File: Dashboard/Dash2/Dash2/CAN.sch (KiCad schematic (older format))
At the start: 20 parts, among them J201 CAN_OUT, J202 CAN_IN, U201 ADM3055E, U202 CDSOT23-T24CAN

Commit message: Add complete layout of the board
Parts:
- C201, C206: Mouser Part Number (none) -> 80-C0805C106K8RAUTO
- C202, C203, C207: Mouser Part Number (none) -> 80-C0805C104K3R
- C204, C208: Mouser Part Number (none) -> 80-C0805X103K1R3316
- C205: Mouser Part Number (none) -> 80-C0805C224J1RECTU
- L201, L202: Mouser Part Number (none) -> 963-BK2125LM182-T
- R201: Mouser Part Number (none) -> 71-CRCW08050000Z0EAC
- R202, R203: Mouser Part Number (none) -> 71-CRCW080559R0FKEA
- U202: Mouser Part Number (none) -> 652-CDSOT23-T24CAN
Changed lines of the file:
@@
 EESchema Schematic File Version 4
-LIBS:Dash2-cache
-EELAYER 26 0
+EELAYER 30 0
 EELAYER END
 $Descr A4 11693 8268
@@
 F 2 "Resistor_SMD:R_0805_2012Metric" V 8130 3550 50  0001 C CNN
 F 3 "" H 8200 3550 50  0001 C CNN
+F 4 "71-CRCW080559R0FKEA" H 8200 3550 50  0001 C CNN "Mouser Part Number"
 	1    8200 3550
 	1    0    0    -1
@@
 F 2 "Resistor_SMD:R_0805_2012Metric" V 7930 3550 50  0001 C CNN
 F 3 "" H 8000 3550 50  0001 C CNN
+F 4 "71-CRCW080559R0FKEA" H 8000 3550 50  0001 C CNN "Mouser Part Number"
 	1    8000 3550
 	1    0    0    -1
@@
 F 2 "Capacitor_SMD:C_0805_2012Metric" H 2150 3350 50  0001 C CNN
 F 3 "" H 2150 3350 50  0001 C CNN
+F 4 "80-C0805C106K8RAUTO " H 2150 3350 50  0001 C CNN "Mouser Part Number"
 	1    2150 3350
 	1    0    0    -1
@@
 F 1 "0.1uF" H 2510 3270 50  0000 L CNN
 F 2 "Capacitor_SMD:C_0805_2012Metric" H 2500 3350 50  0001 C CNN
-F 3 "" H 2500 3350 50  0001 C CNN
+F 3 "~" H 2500 3350 50  0001 C CNN
+F 4 "80-C0805C104K3R " H 2500 3350 50  0001 C CNN "Mouser Part Number"
 	1    2500 3350
 	1    0    0    -1
@@
 F 1 "0.1uF" H 2960 3270 50  0000 L CNN
 F 2 "Capacitor_SMD:C_0805_2012Metric" H 2950 3350 50  0001 C CNN
-F 3 "" H 2950 3350 50  0001 C CNN
+F 3 "~" H 2950 3350 50  0001 C CNN
+F 4 "80-C0805C104K3R " H 2950 3350 50  0001 C CNN "Mouser Part Number"
 	1    2950 3350
 	1    0    0    -1
@@
 F 1 "0.01uF" H 3310 3270 50  0000 L CNN
 F 2 "Capacitor_SMD:C_0805_2012Metric" H 3300 3350 50  0001 C CNN
-F 3 "" H 3300 3350 50  0001 C CNN
+F 3 "~" H 3300 3350 50  0001 C CNN
+F 4 "80-C0805X103K1R3316 " H 3300 3350 50  0001 C CNN "Mouser Part Number"
 	1    3300 3350
 	1    0    0    -1
@@
 F 2 "Capacitor_SMD:C_0805_2012Metric" H 6150 3200 50  0001 C CNN
 F 3 "" H 6150 3200 50  0001 C CNN
+F 4 "80-C0805C106K8RAUTO " H 6150 3200 50  0001 C CNN "Mouser Part Number"
 	1    6150 3200
 	1    0    0    -1
@@
 F 2 "Capacitor_SMD:C_0805_2012Metric" H 5750 3200 50  0001 C CNN
 F 3 "" H 5750 3200 50  0001 C CNN
+F 4 "80-C0805C224J1RECTU " H 5750 3200 50  0001 C CNN "Mouser Part Number"
 	1    5750 3200
 	1    0    0    -1
@@
 F 2 "Inductor_SMD:L_0805_2012Metric" V 5880 3050 50  0001 C CNN
 F 3 "" H 5950 3050 50  0001 C CNN
+F 4 "963-BK2125LM182-T " H 5950 3050 50  0001 C CNN "Mouser Part Number"
 	1    5950 3050
 	0    1    1    0
@@
 F 2 "Inductor_SMD:L_0805_2012Metric" V 5880 3350 50  0001 C CNN
 F 3 "" H 5950 3350 50  0001 C CNN
+F 4 "963-BK2125LM182-T " H 5950 3350 50  0001 C CNN "Mouser Part Number"
 	1    5950 3350
 	0    1    1    0
@@
 F 1 "0.1uF" H 6560 3120 50  0000 L CNN
 F 2 "Capacitor_SMD:C_0805_2012Metric" H 6550 3200 50  0001 C CNN
-F 3 "" H 6550 3200 50  0001 C CNN
+F 3 "~" H 6550 3200 50  0001 C CNN
+F 4 "80-C0805C104K3R " H 6550 3200 50  0001 C CNN "Mouser Part Number"
 	1    6550 3200
 	1    0    0    -1
@@
 F 1 "0.01uF" H 6860 3120 50  0000 L CNN
 F 2 "Capacitor_SMD:C_0805_2012Metric" H 6850 3200 50  0001 C CNN
-F 3 "" H 6850 3200 50  0001 C CNN
+F 3 "~" H 6850 3200 50  0001 C CNN
+F 4 "80-C0805X103K1R3316 " H 6850 3200 50  0001 C CNN "Mouser Part Number"
 	1    6850 3200
 	1    0    0    -1
@@
 F 2 "Resistor_SMD:R_0805_2012Metric" V 5480 4150 50  0001 C CNN
 F 3 "" H 5550 4150 50  0001 C CNN
+F 4 "71-CRCW08050000Z0EAC " H 5550 4150 50  0001 C CNN "Mouser Part Number"
 	1    5550 4150
 	0    -1   -1   0
@@
 F 2 "Package_TO_SOT_SMD:SOT-23W" H 8100 2850 60  0001 C CNN
 F 3 "" H 8100 2850 60  0001 C CNN
+F 4 "652-CDSOT23-T24CAN " H 8100 2850 50  0001 C CNN "Mouser Part Number"
 	1    8100 2850
 	1    0    0    -1

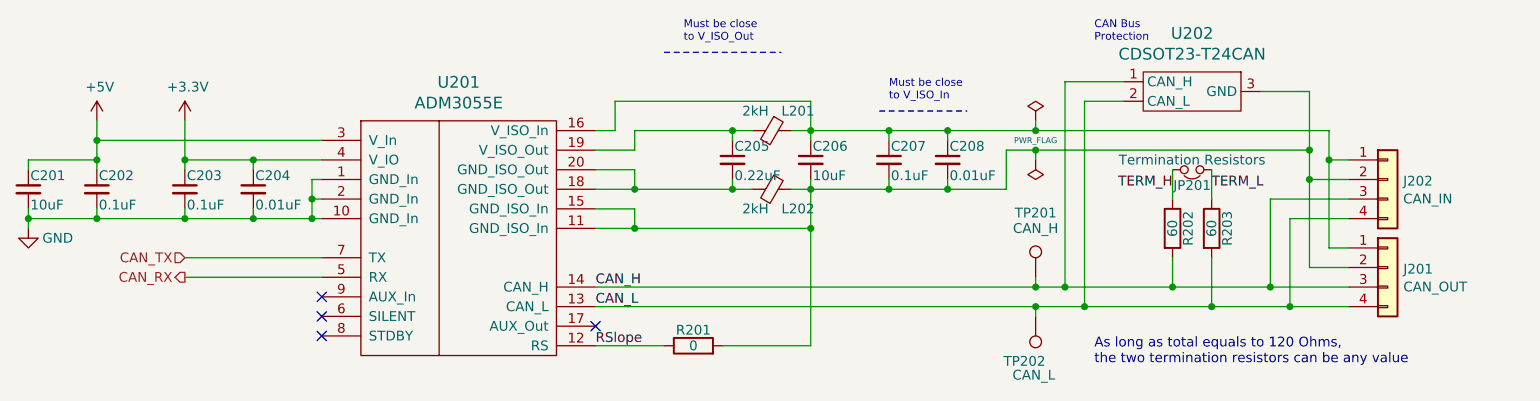
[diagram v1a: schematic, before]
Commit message: Add LED board and timing circuitry. The LED board is not yet integrated with the Dash.
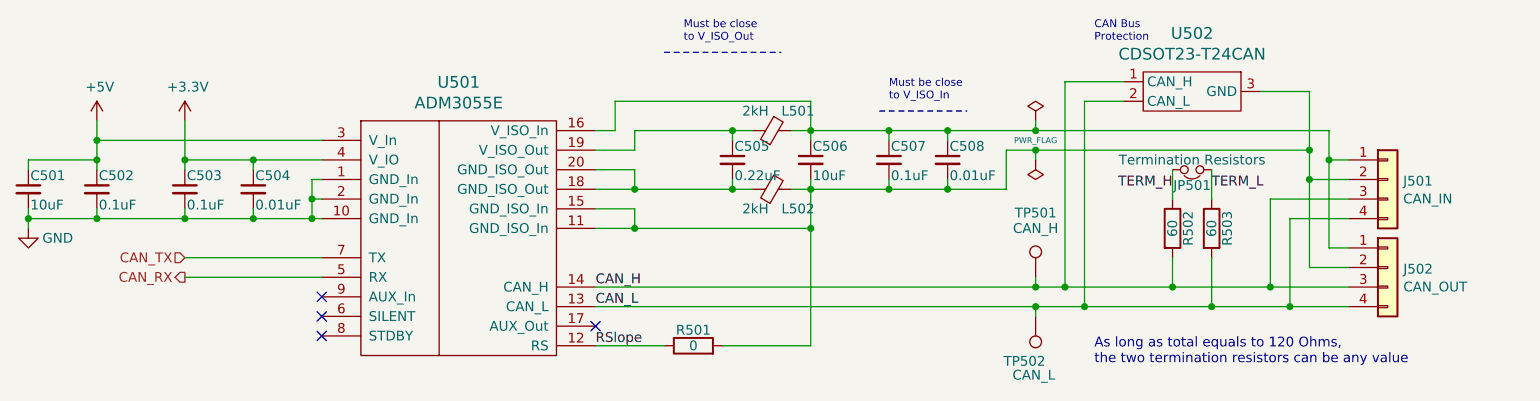
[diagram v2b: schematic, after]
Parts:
- renumbered J202 to J201, J201 to J202
